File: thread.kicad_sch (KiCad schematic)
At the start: 32 parts, among them J3002 TC2050, J3003 Conn_01x06_Pin, J3004 SMA-KWE901, SW3001 SW_MEC_5E, U3001 nRF52840, X3001 32.768kHz, X3002 25MHz

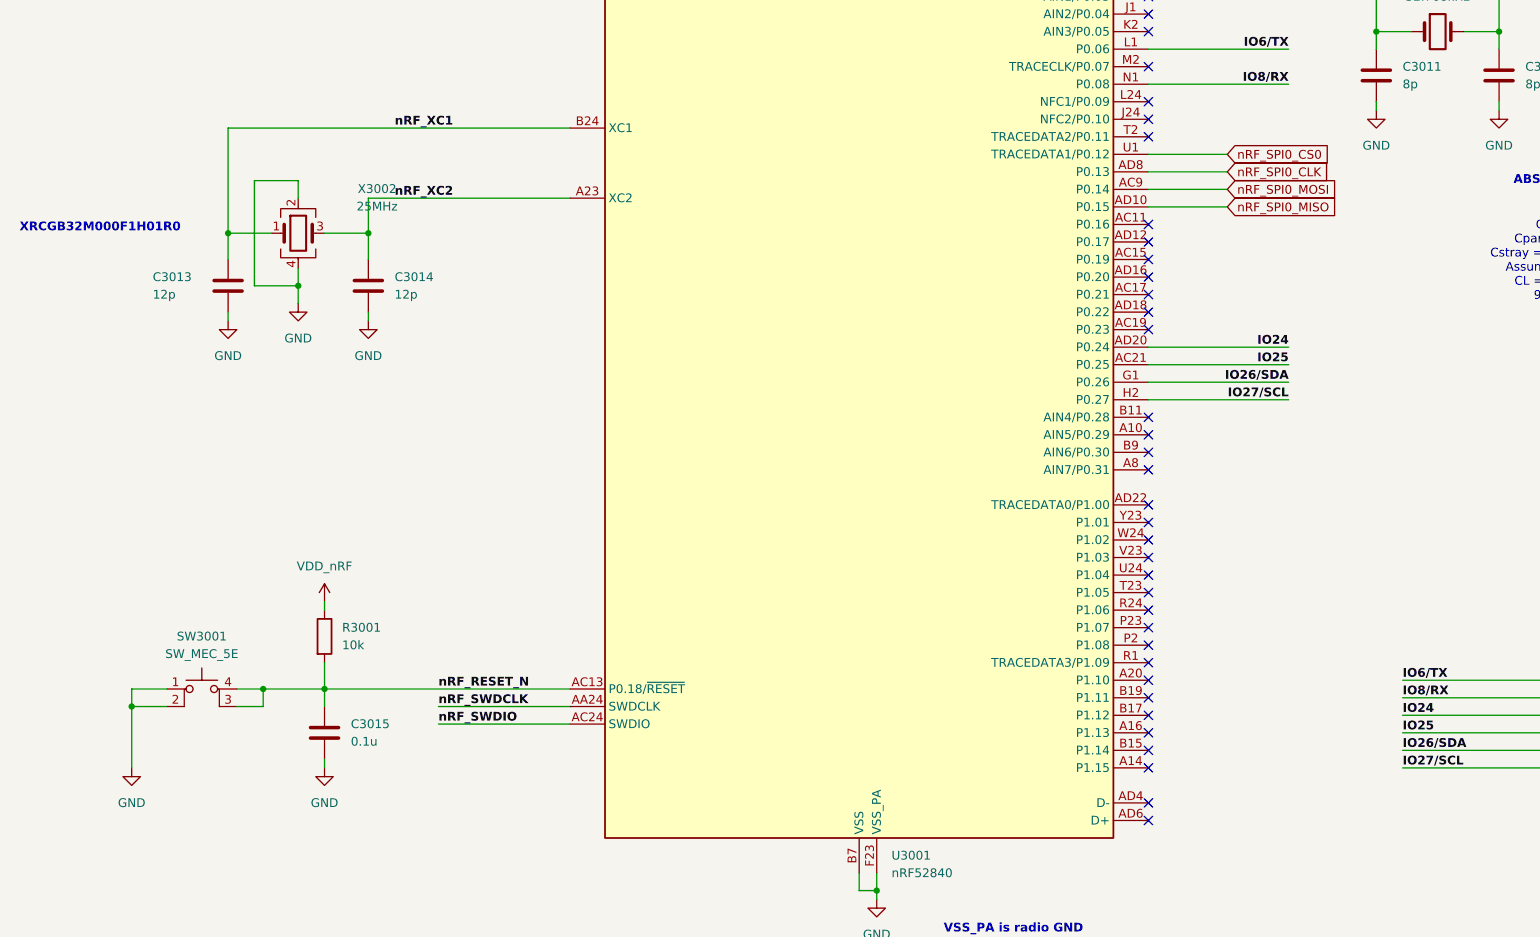
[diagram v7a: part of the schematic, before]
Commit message: Added necessary nRF52840 SPI logic circuitry and GPIOs. Also added pinmux
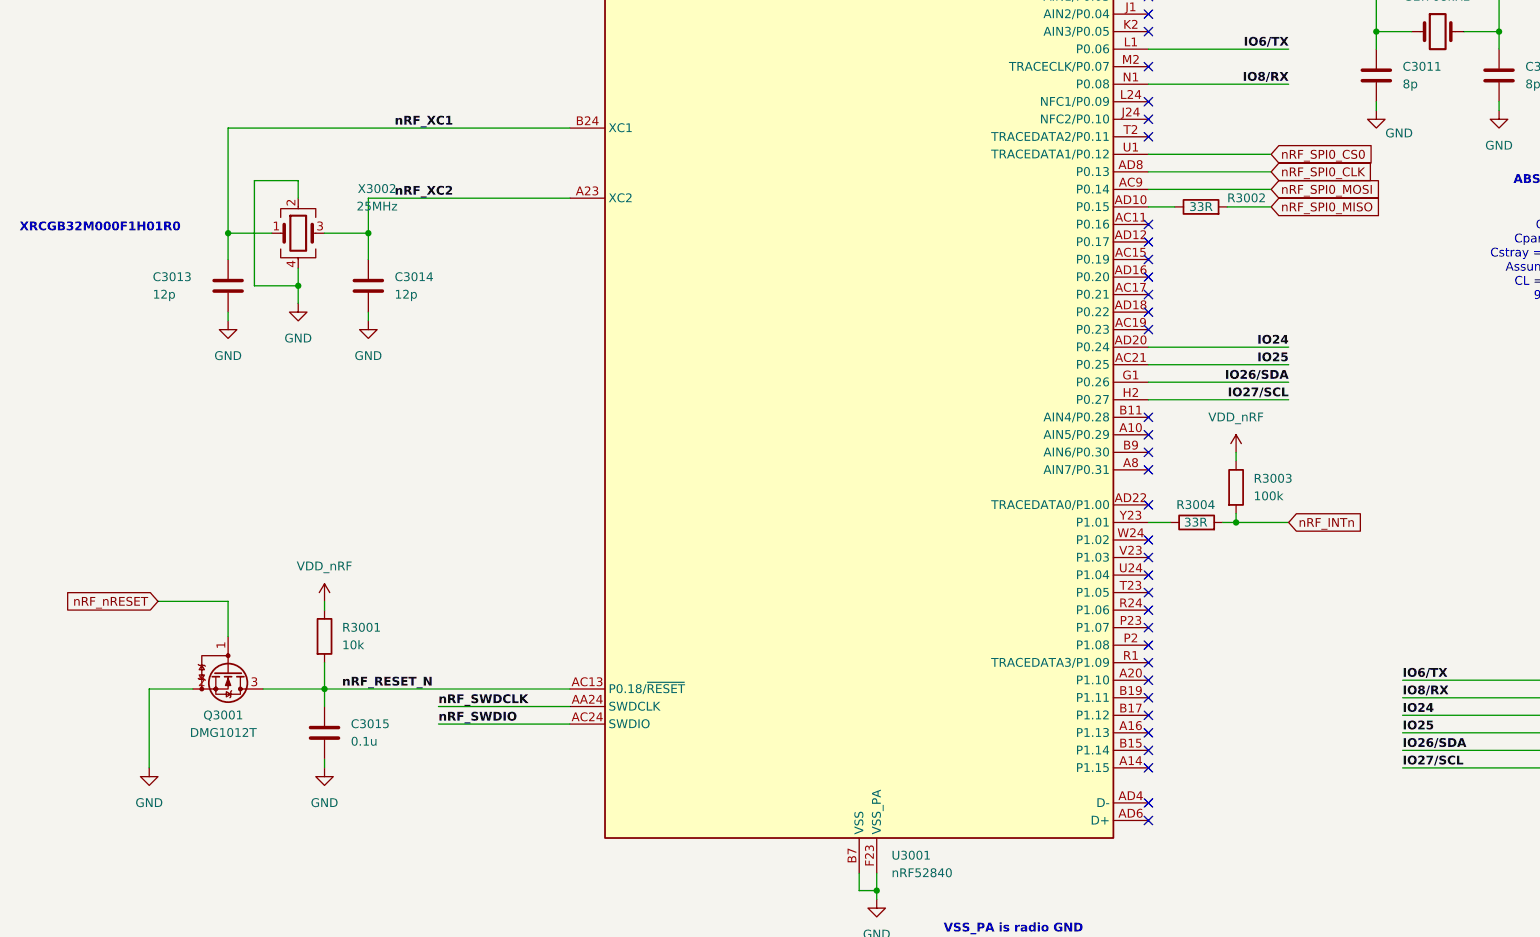
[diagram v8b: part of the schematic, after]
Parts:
- removed SW3001: SW_MEC_5E, symbol Switch:SW_MEC_5E
- added Q3001: DMG1012T, Package_TO_SOT_SMD:SOT-523, symbol Transistor_FET:DMG1012T
- added R3002, R3004: 33R, symbol Device:R
- added R3003: 100k, symbol Device:R
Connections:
- net GND: now also Q3001.2 (S)
- net VDD_nRF: now also R3003.1
- net nRF_RESET_N: now also Q3001.3 (D)
- net nRF_SPI0_MISO: now also R3002.2; no longer U3001.AD10 (P0.15)
- net at U3001.Y23 (P1.01): now also R3004.1
- new net: R3002.1, U3001.AD10 (P0.15)
- new net nRF_INTn: R3003.2, R3004.2
- new net nRF_nRESET: Q3001.1 (G)
- no-connect marks 45 -> 44
